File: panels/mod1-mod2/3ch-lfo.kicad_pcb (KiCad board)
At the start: 2 copper layers, 19.8 x 128.5 mm, 0 parts

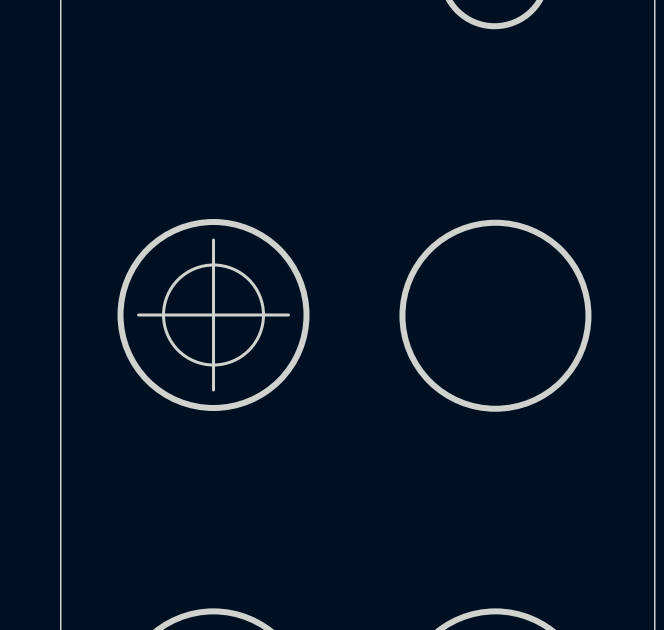
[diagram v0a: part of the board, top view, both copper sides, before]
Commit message: mod2 firmwares, new faceplates
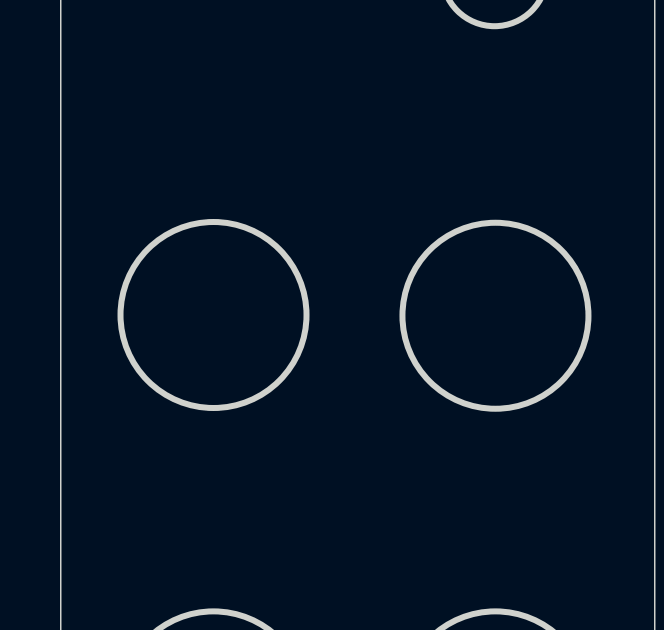
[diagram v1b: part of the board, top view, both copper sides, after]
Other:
- outline, holes or cut-outs redrawn
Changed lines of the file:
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@@
-	)
-	(gr_circle
-		(center 60.9362 127.4138)
-		(end 62.60287 127.4138)
-		(stroke
-			(width 0.1)
-			(type solid)
-		)
-		(fill no)
-		(layer "Edge.Cuts")
 	)
 	(gr_circle
@@
 		(layer "Edge.Cuts")
 	)
-	(gr_line
-		(start 58.4362 127.4138)
-		(end 63.4362 127.4138)
-		(stroke
-			(width 0.1)
-			(type solid)
-		)
-		(layer "Edge.Cuts")
-	)
 	(gr_arc
 		(start 59.654 32.8656)
@@
 			(type solid)
 		)
-		(layer "Edge.Cuts")
-	)
-	(gr_line
-		(start 60.9362 124.9138)
-		(end 60.9362 129.9138)
-		(stroke
-			(width 0.1)
-			(type solid)
-		)
